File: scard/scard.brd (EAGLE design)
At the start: 47 x 86.5 mm, 70 parts, among them P1 TPS548A20, Q1 FDN360P, T1 LT3652, X1 COAX, X2 1365-20

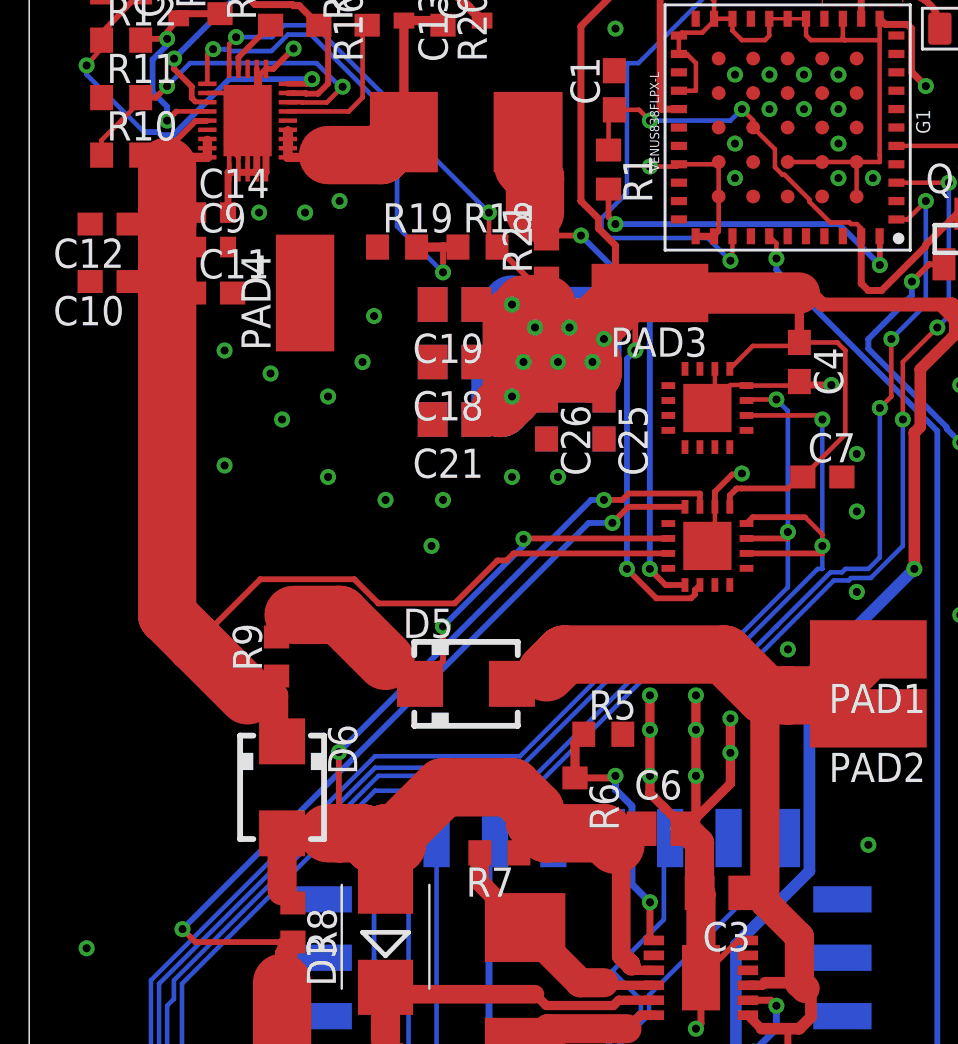
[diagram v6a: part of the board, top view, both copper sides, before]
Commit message: fixed misplaced current measurement traces at Brent's suggestion
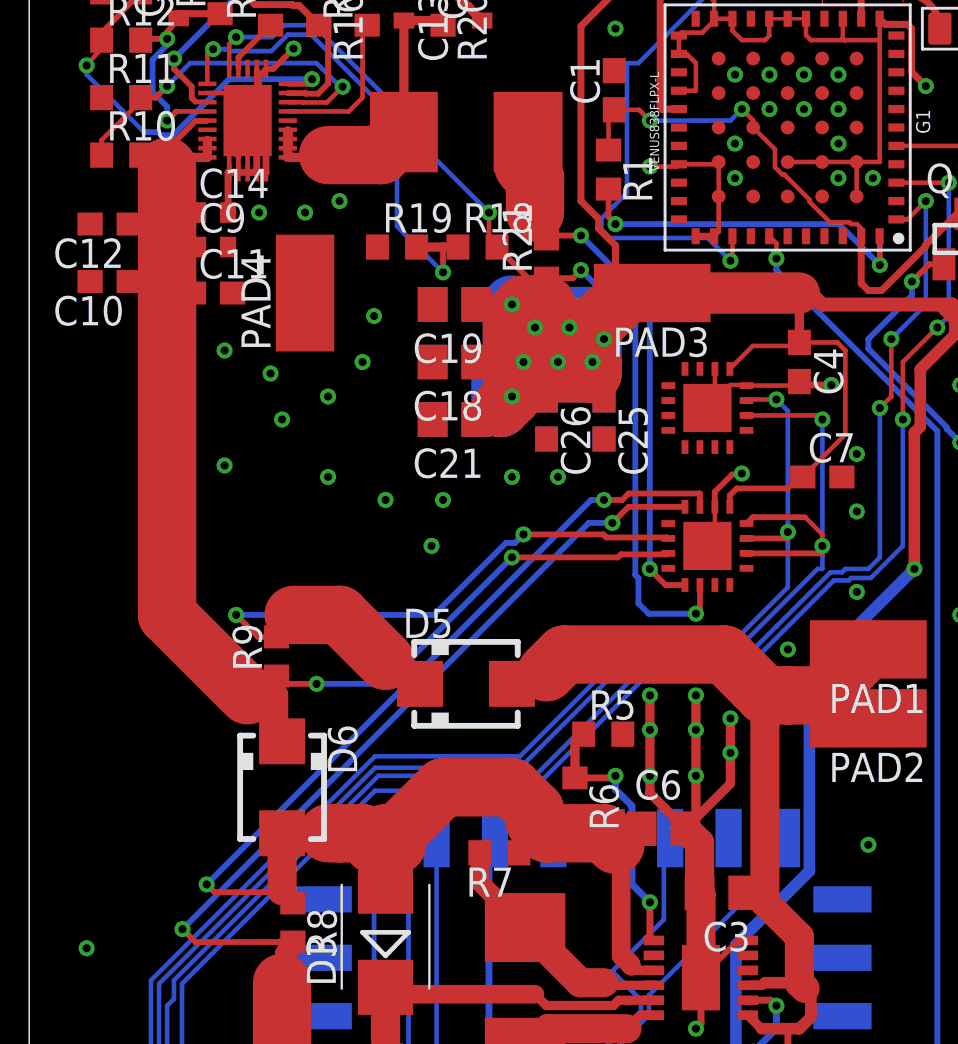
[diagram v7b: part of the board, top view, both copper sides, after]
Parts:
- moved PAD3 0.10 mm to (26.6, 63.0)
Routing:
- net VBATT_CUR: track 60.5 -> 68.6 mm
- net SYS_UNREG_CUR: track 22.5 -> 30.5 mm
- net +3V3: track 243.4 -> 247.5 mm
- net VSYS_UNREG: track 66.9 -> 63.0 mm, vias 0 -> 2

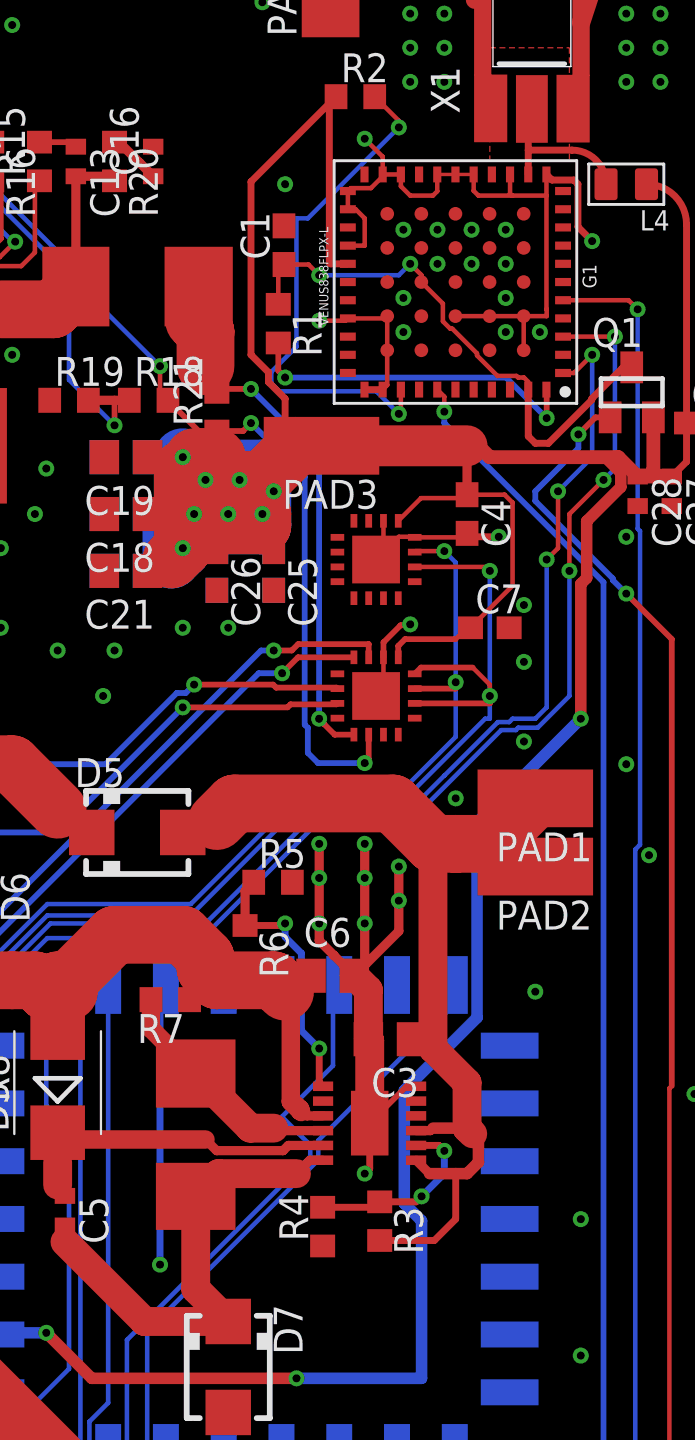
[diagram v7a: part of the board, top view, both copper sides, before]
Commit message: added new 10uH inductor due to original inductor going out of stock. Updated CAM files. Fixed issue with GPS pads having no thermals
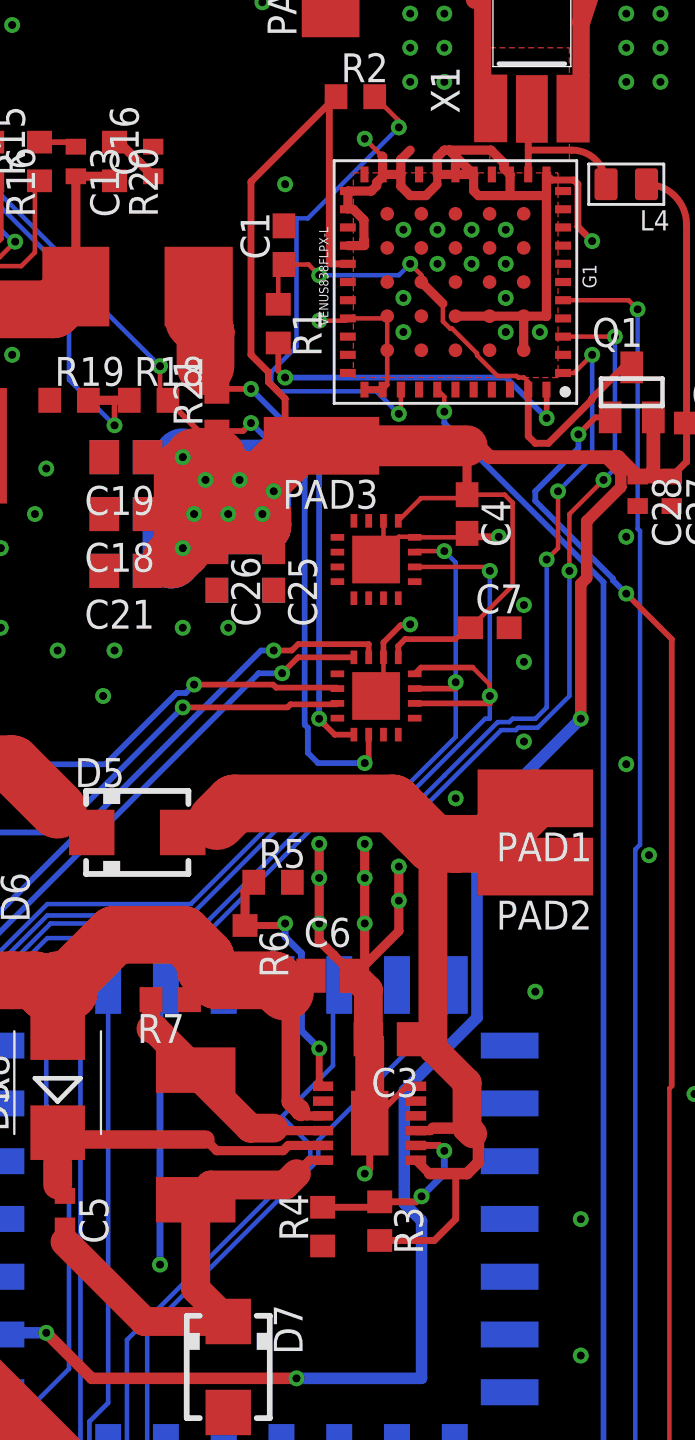
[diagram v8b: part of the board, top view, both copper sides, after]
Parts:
- L2: device calsat:SRP7028A -> calsat:SRP7030
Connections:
- removed net N$4: C5.2, D7.C, L2.1, T1.12
- new net N$18: C5.2, D7.C, L2.P$1, T1.12
- net N$6: now also L2.P$2; no longer L2.2
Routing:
- net GND: track 136.3 -> 160.3 mm
- net N$4: track 22.3 -> 0.00 mm
- net N$18: track 0.00 -> 22.2 mm
